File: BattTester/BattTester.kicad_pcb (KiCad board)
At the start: 2 copper layers, 25 parts, among them J1 Battery, J2 SD_Card, J3 PWR, J4 UPDI, Q1 IRLZ44N, U1 LT1286CN8, U2 ATtiny1624-SS, U3 LD1086DT33, U4 LM358AN

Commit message: Finish routing
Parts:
- added REF**: MountingHole_3.2mm_M3, MountingHole:MountingHole_3.2mm_M3, F.Cu at (208.3, 68.6)
- added REF**: MountingHole_3.2mm_M3, MountingHole:MountingHole_3.2mm_M3, F.Cu at (142.9, 68.6)
- added REF**: MountingHole_3.2mm_M3, MountingHole:MountingHole_3.2mm_M3, F.Cu at (142.9, 121.9)
- added REF**: MountingHole_3.2mm_M3, MountingHole:MountingHole_3.2mm_M3, F.Cu at (234.9, 121.9)
- U1, U4: footprint BattTester:Texas_Instruments-P0008A-0-0-MFG -> BattTester:DIP8
- moved U1 4.83 mm to (168.8, 102.9)
- moved U4 4.83 mm to (170.9, 81.3)
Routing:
- net /SPI-CS1: track 0.00 -> 32.5 mm
- net /SPI-MOSI: track 0.00 -> 28.1 mm, vias 0 -> 2
- net +3V3: track 97.0 -> 120.4 mm
- net /SPI-SCK: track 14.1 -> 30.5 mm
- net /WRPrt: track 0.00 -> 15.1 mm
- net /SPI-MISO: track 13.9 -> 26.9 mm
- net /SDDet: track 0.00 -> 11.2 mm
- net Net-(D2-Pad2): track 0.00 -> 4.79 mm
- net Net-(D1-Pad2): track 0.00 -> 4.79 mm
- net GND: track 69.7 -> 71.3 mm, vias 2 -> 8
- net +9V: track 109.5 -> 110.1 mm
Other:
- board outline added: 99.7 x 61 mm

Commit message: minor name fix
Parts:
- U1: value LT1286CN8 -> LTC1286CN8

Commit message: fix updi header
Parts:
- moved R6 2.16 mm to (207.0, 114.0)
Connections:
- J4 pad 1: +3V3 -> Net-(J4-Pad1)
- J4 pad 2: Net-(J4-Pad2) -> GND
- J4 pad 3: GND -> +3V3
- R6 pad 2: Net-(J4-Pad2) -> Net-(J4-Pad1)
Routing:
- net Net-(J4-Pad1): track 0.00 -> 4.20 mm
- net Net-(J4-Pad2): track 4.04 -> 0.00 mm
- net +3V3: track 120.4 -> 122.4 mm
- net /RESET: track 9.91 -> 9.01 mm
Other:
- board text added: "2S Lipo Battery Tester Designed by Alan Hsu v0.1"
- board text added: "3V3"
- board text added: "Battery VIN <9V"
- board text added: "CURRENT SHUNT"
- board text added: "GND"
- board text added: "HEATSINK THIS MOSFET"
- board text added: "UPDI"

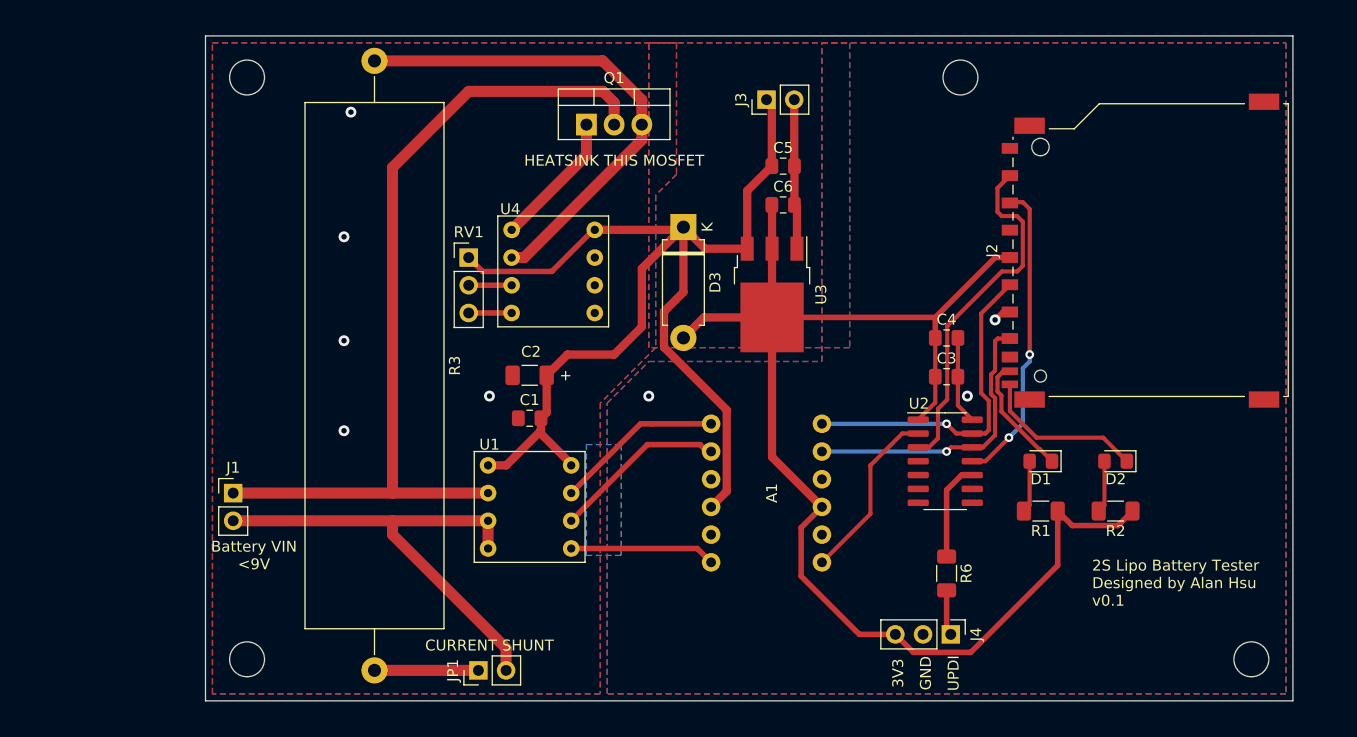
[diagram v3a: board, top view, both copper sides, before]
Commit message: cutoff mosfet and higher power Rload
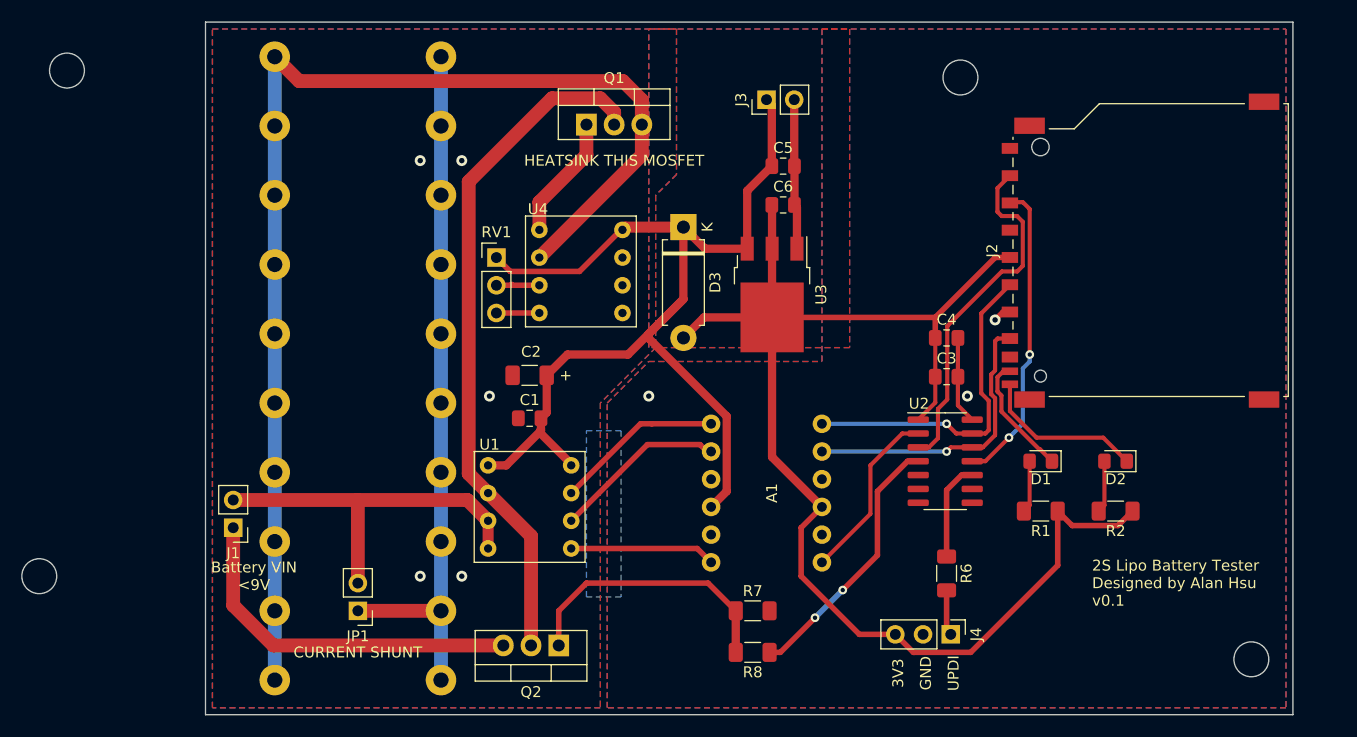
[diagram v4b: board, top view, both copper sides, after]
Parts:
- added Q2: IRF4905, Package_TO_SOT_THT:TO-220-3_Vertical, F.Cu at (171.4, 120.7)
- added R7: 10K, Resistor_SMD:R_1206_3216Metric_Pad1.30x1.75mm_HandSolder, F.Cu at (189.2, 117.5)
- added R8: 100R, Resistor_SMD:R_1206_3216Metric_Pad1.30x1.75mm_HandSolder, F.Cu at (189.2, 121.3)
- R3: value 1R, 5W -> 1R, 40-50W; footprint Resistor_THT:R_Axial_Power_L48.0mm_W12.5mm_P55.88mm -> BattTester:10xParallel_R_Axial_DIN0614_L14.3mm_D5.7mm_P15.24mm_Horizontal; moved to B.Cu
- moved R3 57.5 mm to (145.4, 123.8), turned to 0 degrees
- moved REF** 20.5 mm to (123.8, 114.3)
- moved REF** 16.5 mm to (126.4, 67.9)
- moved JP1 12.3 mm to (153.0, 117.5), turned to 180 degrees
- moved J1 3.17 mm to (141.6, 109.9), turned to 180 degrees
- moved RV1 2.54 mm to (165.7, 85.1)
- moved U4 2.54 mm to (173.5, 81.3)
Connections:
- J1 pad 1: /B+ -> /BIN+
- U2 pad 4: (no net) -> /CUTOFF
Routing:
- net Net-(Q1-Pad3): track 46.3 -> 110.8 mm
- net Net-(JP1-Pad1): track 9.53 -> 64.8 mm
- net /BIN+: track 0.00 -> 33.4 mm
- net Net-(Q2-Pad1): track 0.00 -> 25.3 mm
- net /CUTOFF: track 0.00 -> 24.3 mm, vias 0 -> 2
- net /B+: track 78.9 -> 63.1 mm
- net GND: track 71.3 -> 61.7 mm
- net +9V: track 110.1 -> 103.0 mm
- net Net-(Q1-Pad1): track 12.5 -> 11.4 mm
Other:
- board size 99.7 x 61 mm -> 99.7 x 63.5 mm

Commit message: silkscreen update
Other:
- board text added: "10X PARALLEL 5W 10R RESISTORS"

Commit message: work on things
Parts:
- moved REF** 58.4 mm to (184.8, 67.3)
- moved REF** 57.2 mm to (180.3, 123.2)
- moved REF** 1.27 mm to (208.3, 67.3)
- moved REF** 1.27 mm to (234.9, 123.2)

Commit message: Fix #1
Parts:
- removed REF** (x4): MountingHole_3.2mm_M3, MountingHole:MountingHole_3.2mm_M3
- added Q3: 2N7002, Package_TO_SOT_SMD:SOT-23, F.Cu at (184.2, 120.7)
- added R9: 10K, Resistor_SMD:R_1206_3216Metric_Pad1.30x1.75mm_HandSolder, F.Cu at (188.6, 120.7)
- R7: moved to B.Cu
- moved R7 21.3 mm to (168.9, 123.8), turned to 180 degrees
- moved R8 4.49 mm to (193.7, 121.9)
- moved J3 3.18 mm to (193.7, 70.6)
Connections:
- R7 pad 2: GND -> /BIN+
- R8 pad 2: Net-(Q2-Pad1) -> Net-(Q3-Pad1)
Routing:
- net Net-(Q3-Pad1): track 0.00 -> 7.34 mm
- net /BIN+: track 33.4 -> 37.0 mm
- net /CUTOFF: track 24.3 -> 22.5 mm
- net GND: track 61.7 -> 63.0 mm
- net Net-(Q2-Pad1): track 25.3 -> 24.3 mm
- net +9V: track 103.0 -> 103.9 mm

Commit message: update gerbers, finish firmware
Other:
- board text added: "2S Lipo Battery Tester Designed by Alan Hsu v1.0"
- board text removed: "2S Lipo Battery Tester Designed by Alan Hsu v0.1"
